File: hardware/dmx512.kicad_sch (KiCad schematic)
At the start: 18 parts, among them J16 Conn_01x06, J17 Conn_01x06, SW1 SW_DIP_x10, U4 MCP23017T-E/SS, U5 CA-IS3092W

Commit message: removed Art-Net
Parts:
- J16, J17: footprint Connector_JST:JST_PH_B6B-PH-K_1x06_P2.00mm_Vertical -> Connector_JST:JST_PH_B6B-PH-SM4-TB_1x06-1MP_P2.00mm_Vertical; LCSC C274409 -> (none)
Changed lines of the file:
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@@
 			)
 		)
-		(property "Footprint" "Connector_JST:JST_PH_B6B-PH-K_1x06_P2.00mm_Vertical"
+		(property "Footprint" "Connector_JST:JST_PH_B6B-PH-SM4-TB_1x06-1MP_P2.00mm_Vertical"
 			(at 38.1 78.74 0)
 			(effects
@@
 			)
 		)
-		(property "LCSC" "C274409"
+		(property "LCSC" ""
 			(at 38.1 78.74 0)
 			(effects
@@
 			)
 		)
-		(property "Footprint" "Connector_JST:JST_PH_B6B-PH-K_1x06_P2.00mm_Vertical"
+		(property "Footprint" "Connector_JST:JST_PH_B6B-PH-SM4-TB_1x06-1MP_P2.00mm_Vertical"
 			(at 38.1 53.34 0)
 			(effects
@@
 			)
 		)
-		(property "LCSC" "C274409"
+		(property "LCSC" ""
 			(at 38.1 53.34 0)
 			(effects

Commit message: clean up
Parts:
- added R43: 10k, Resistor_SMD:R_0603_1608Metric, symbol Device:R
- J2: renamed from J16; LCSC (none) -> C471518
- J3: renamed from J17; LCSC (none) -> C471518
- R9: renamed from R23; footprint Resistor_SMD:R_0805_2012Metric_Pad1.20x1.40mm_HandSolder -> Resistor_SMD:R_0805_2012Metric
- renumbered C23 to C10, C18 to C5, C19 to C6, C20 to C7, C21 to C8, C22 to C9, R24 to R10, R25 to R11, R26 to R12, R27 to R13, R22 to R8, U4 to U2, U5 to U3
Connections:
- net DMX_DE/~{RE}: now also R43.1
- net GND: now also R43.2
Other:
- note added: "Failsafe Bias"
- note removed: "Failsafe"

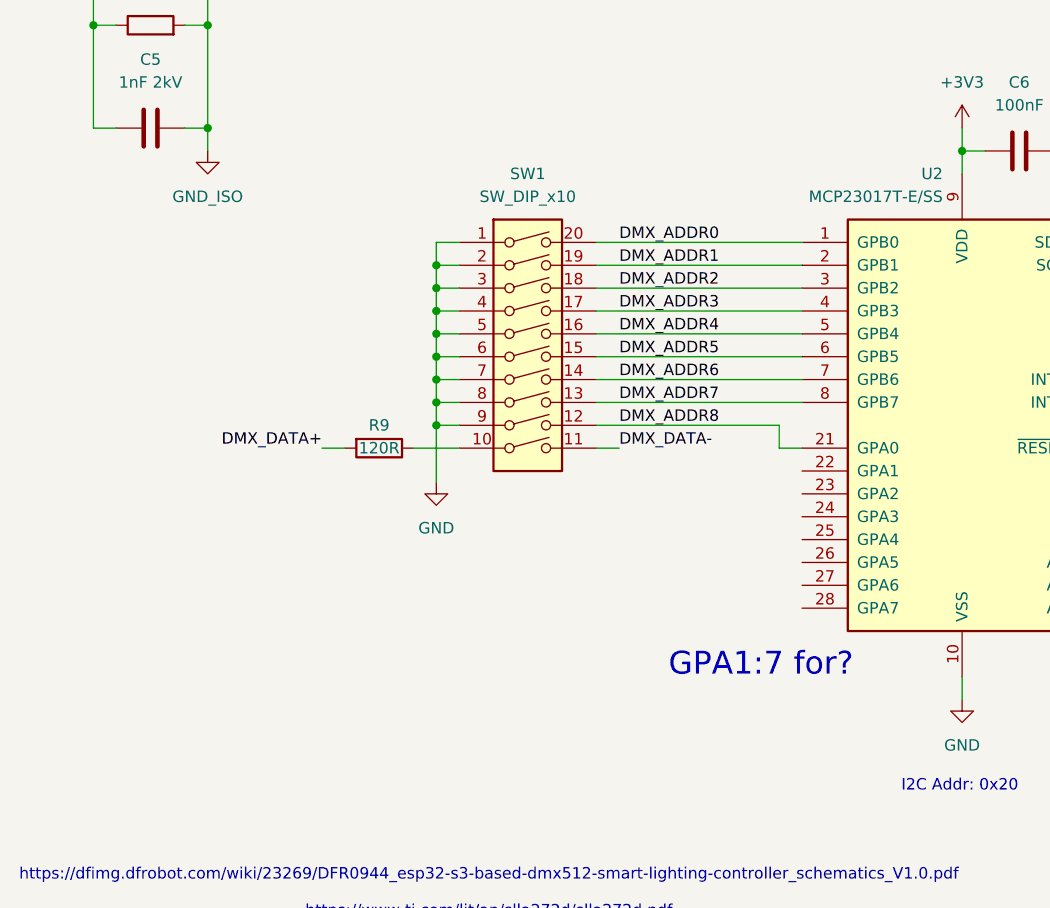
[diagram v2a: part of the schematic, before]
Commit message: updating thermistor and GPIO expander
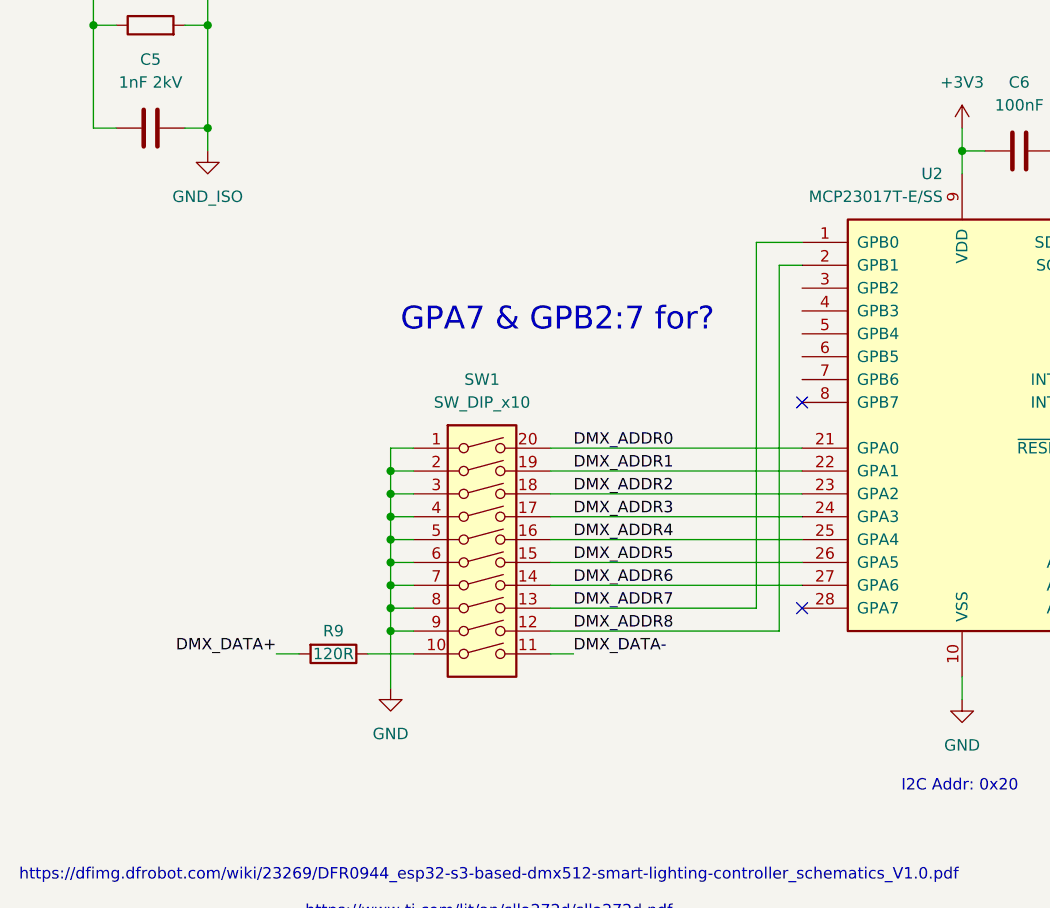
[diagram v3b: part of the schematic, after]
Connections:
- net DMX_ADDR0: now also U2.21 (GPA0); no longer U2.1 (GPB0)
- net DMX_ADDR1: now also U2.22 (GPA1); no longer U2.2 (GPB1)
- net DMX_ADDR2: now also U2.23 (GPA2); no longer U2.3 (GPB2)
- net DMX_ADDR3: now also U2.24 (GPA3); no longer U2.4 (GPB3)
- net DMX_ADDR4: now also U2.25 (GPA4); no longer U2.5 (GPB4)
- net DMX_ADDR5: now also U2.26 (GPA5); no longer U2.6 (GPB5)
- net DMX_ADDR6: now also U2.27 (GPA6); no longer U2.7 (GPB6)
- net DMX_ADDR7: now also U2.1 (GPB0); no longer U2.8 (GPB7)
- net DMX_ADDR8: now also U2.2 (GPB1); no longer U2.21 (GPA0)
- no-connect marks 1 -> 3
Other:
- note added: "GPA7 & GPB2:7 for?"
- note removed: "GPA1:7 for?"
- moved on the sheet: R9, SW1

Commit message: adding snubbers, starting placement
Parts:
- removed R9: 120R, Resistor_SMD:R_0805_2012Metric, symbol Device:R
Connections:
- net DMX_DATA-: no longer SW1.11
- net GND: now also SW1.10
- new net WIFI_~{ENABLE}: SW1.11
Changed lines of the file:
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@@
+	)
+	(junction
+		(at 78.74 165.1)
+		(diameter 0)
+		(color 0 0 0 0)
 	)
 	(junction
@@
 	(wire
 		(pts
+			(xy 194.31 38.1) (xy 194.31 40.64)
+		)
+		(stroke
+			(width 0)
+			(type default)
+		)
+	)
+	(wire
+		(pts
+			(xy 78.74 162.56) (xy 81.28 162.56)
+		)
+		(stroke
+			(width 0)
+			(type default)
+		)
+	)
+	(wire
+		(pts
+			(xy 144.78 77.47) (xy 144.78 80.01)
+		)
+		(stroke
+			(width 0)
+			(type default)
+		)
+	)
+	(wire
+		(pts
 			(xy 96.52 165.1) (xy 99.06 165.1)
 		)
@@
 	(wire
 		(pts
-			(xy 194.31 38.1) (xy 194.31 40.64)
-		)
-		(stroke
-			(width 0)
-			(type default)
-		)
-	)
-	(wire
-		(pts
-			(xy 78.74 162.56) (xy 81.28 162.56)
-		)
-		(stroke
-			(width 0)
-			(type default)
-		)
-	)
-	(wire
-		(pts
-			(xy 144.78 77.47) (xy 144.78 80.01)
+			(xy 78.74 165.1) (xy 81.28 165.1)
 		)
 		(stroke
@@
 	(wire
 		(pts
+			(xy 78.74 165.1) (xy 78.74 168.91)
+		)
+		(stroke
+			(width 0)
+			(type default)
+		)
+	)
+	(wire
+		(pts
 			(xy 58.42 95.25) (xy 58.42 73.66)
 		)
@@
 	(wire
 		(pts
-			(xy 76.2 165.1) (xy 81.28 165.1)
-		)
-		(stroke
-			(width 0)
-			(type default)
-		)
-	)
-	(wire
-		(pts
 			(xy 43.18 73.66) (xy 58.42 73.66)
 		)
@@
 	(wire
 		(pts
-			(xy 66.04 165.1) (xy 68.58 165.1)
-		)
-		(stroke
-			(width 0)
-			(type default)
-		)
-	)
-	(wire
-		(pts
 			(xy 152.4 109.22) (xy 154.94 109.22)
 		)
@@
 	(wire
 		(pts
+			(xy 99.06 167.64) (xy 101.6 167.64)
+		)
+		(stroke
+			(width 0)
+			(type default)
+		)
+	)
+	(wire
+		(pts
 			(xy 43.18 78.74) (xy 60.96 78.74)
 		)
@@
 	(wire
 		(pts
-			(xy 78.74 162.56) (xy 78.74 168.91)
+			(xy 78.74 162.56) (xy 78.74 165.1)
 		)
 		(stroke
@@
 		(pts
 			(xy 58.42 95.25) (xy 58.42 106.68)
+		)
+		(stroke
+			(width 0)
+			(type default)
+		)
+	)
+	(wire
+		(pts
+			(xy 99.06 165.1) (xy 99.06 167.64)
 		)
 		(stroke
@@
 		)
 	)
-	(label "DMX_DATA+"
-		(at 66.04 165.1 180)
-		(effects
-			(font
-				(size 1.27 1.27)
-			)
-			(justify right bottom)
-		)
-	)
 	(label "DMX_AUX+"
 		(at 60.96 83.82 0)
@@
 			)
 			(justify right bottom)
-		)
-	)
-	(label "DMX_DATA-"
-		(at 99.06 165.1 0)
-		(effects
-			(font
-				(size 1.27 1.27)
-			)
-			(justify left bottom)
 		)
 	)
@@
 		(shape output)
 		(at 226.06 72.39 0)
+		(effects
+			(font
+				(size 1.27 1.27)
+			)
+			(justify left)
+		)
+	)
+	(hierarchical_label "WIFI_~{ENABLE}"
+		(shape output)
+		(at 101.6 167.64 0)
 		(effects
 			(font
@@
 					(unit 1)
 				)
-			)
-		)
-	)
-	(symbol
-		(lib_id "Device:R")
-		(at 72.39 165.1 270)
-		(unit 1)
-		(exclude_from_sim no)
-		(in_bom yes)
-		(on_board yes)
-		(dnp no)
-		(property "Reference" "R9"
-			(at 72.39 162.56 90)
-			(effects
-				(font
-					(size 1.27 1.27)
-				)
-			)
-		)
-		(property "Value" "120R"
-			(at 72.39 165.1 90)
-			(effects
-				(font
-					(size 1.27 1.27)
-				)
-			)
-		)
-		(property "Footprint" "Resistor_SMD:R_0805_2012Metric"
-			(at 72.39 163.322 90)
-			(effects
-				(font
-					(size 1.27 1.27)
-				)
-				(hide yes)
-			)
-		)
-		(property "Datasheet" "~"
-			(at 72.39 165.1 0)
-			(effects
-				(font
-					(size 1.27 1.27)
-				)
-				(hide yes)
-			)
-		)
-		(property "Description" "Resistor"
-			(at 72.39 165.1 0)
-			(effects
-				(font
-					(size 1.27 1.27)
-				)
-				(hide yes)
-			)
-		)
-		(property "MFR" ""
-			(at 72.39 165.1 90)
-			(effects
-				(font
-					(size 1.27 1.27)
-				)
-				(hide yes)
-			)
-		)
-		(property "MPN" ""
-			(at 72.39 165.1 90)
-			(effects
-				(font
-					(size 1.27 1.27)
-				)
-				(hide yes)
-			)
-		)
-		(pin "1"
-		)
-		(pin "2"
-		)
-		(instances
-			(project "emf_beacon"
-				(path "/0654b480-d862-4382-88d5-1ac411bf5574/ef912ffd-e5d9-46a9-9fff-0bf3d4ccd370"
-					(reference "R9")
-					(unit 1)
-				)

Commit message: updating PSUs
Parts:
- C10, C7: LCSC (none) -> C15850
- C5: footprint Capacitor_SMD:C_1808_4520Metric -> Capacitor_SMD:C_1206_3216Metric; LCSC (none) -> C9196
- C6, C8, C9: LCSC (none) -> C14663
- J2, J3: Rotation_offset (none) -> 180
- R10, R11: LCSC (none) -> C23162
- R12, R13, R43: LCSC (none) -> C21190
- R8: LCSC (none) -> C17927
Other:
- note added: "Make a symbol for this"
- note added: "WiFi_~{EN} via GPIO expander?"
- note removed: "May need to actually make a symbol for this"

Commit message: some jlc cleanup
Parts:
- R12, R13, R43: LCSC C21190 -> C25804
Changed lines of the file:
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@@
 			)
 		)
-		(property "LCSC" "C21190"
+		(property "LCSC" "C25804"
 			(at 223.52 78.74 0)
 			(effects
@@
 			)
 		)
-		(property "LCSC" "C21190"
+		(property "LCSC" "C25804"
 			(at 168.91 142.24 90)
 			(effects
@@
 			)
 		)
-		(property "LCSC" "C21190"
+		(property "LCSC" "C25804"
 			(at 168.91 129.54 90)
 			(effects

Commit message: tweaking lcsc part numbers
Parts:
- C10, C7: value 10uF -> 10uF 25V
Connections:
- net +3V3: now also U3.7 (PV)
- no-connect marks 3 -> 2
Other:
- note added: "Make a symbol for CA-IS3092W CA-IS3092VW"
- note added: "OUT OF STOCK!"
- note removed: "Make a symbol for this"
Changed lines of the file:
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@@
 		(company "Wires & Bits")
 	)
-	(text "Make a symbol for this"
+	(text "Make a symbol for\nCA-IS3092W\nCA-IS3092VW"
 		(exclude_from_sim no)
 		(at 198.628 99.822 0)
@@
 		)
 	)
+	(text "OUT OF\nSTOCK!"
+		(exclude_from_sim no)
+		(at 211.074 56.896 0)
+		(effects
+			(font
+				(size 2.54 2.54)
+				(color 255 0 0 1)
+			)
+		)
+	)
 	(text "ESD\nProtection"
 		(exclude_from_sim no)
@@
 	)
 	(no_connect
-		(at 214.63 80.01)
-	)
-	(no_connect
 		(at 124.46 137.16)
 	)
@@
 	(wire
 		(pts
+			(xy 214.63 80.01) (xy 217.17 80.01)
+		)
+		(stroke
+			(width 0)
+			(type default)
+		)
+	)
+	(wire
+		(pts
 			(xy 55.88 106.68) (xy 58.42 106.68)
 		)
@@
 			)
 		)
-		(property "Value" "10uF"
+		(property "Value" "10uF 25V"
 			(at 241.3 48.2599 0)
 			(effects
@@
 	)
 	(symbol
+		(lib_id "power:+3V3")
+		(at 217.17 80.01 270)
+		(unit 1)
+		(exclude_from_sim no)
+		(in_bom yes)
+		(on_board yes)
+		(dnp no)
+		(fields_autoplaced yes)
+		(property "Reference" "#PWR073"
+			(at 213.36 80.01 0)
+			(effects
+				(font
+					(size 1.27 1.27)
+				)
+				(hide yes)
+			)
+		)
+		(property "Value" "+3V3"
+			(at 220.98 80.0099 90)
+			(effects
+				(font
+					(size 1.27 1.27)
+				)
+				(justify left)
+			)
+		)
+		(property "Footprint" ""
+			(at 217.17 80.01 0)
+			(effects
+				(font
+					(size 1.27 1.27)
+				)
+				(hide yes)
+			)
+		)
+		(property "Datasheet" ""
+			(at 217.17 80.01 0)
+			(effects
+				(font
+					(size 1.27 1.27)
+				)
+				(hide yes)
+			)
+		)
+		(property "Description" "Power symbol creates a global label with name \"+3V3\""
+			(at 217.17 80.01 0)
+			(effects
+				(font
+					(size 1.27 1.27)
+				)
+				(hide yes)
+			)
+		)
+		(pin "1"
+		)
+		(instances
+			(project "emf_beacon"
+				(path "/0654b480-d862-4382-88d5-1ac411bf5574/ef912ffd-e5d9-46a9-9fff-0bf3d4ccd370"
+					(reference "#PWR073")
+					(unit 1)
+				)
+			)
+		)
+	)
+	(symbol
 		(lib_id "Device:C")
 		(at 223.52 46.99 0)
@@
 			)
 		)
-		(property "Value" "10uF"
+		(property "Value" "10uF 25V"
 			(at 157.48 48.2599 0)
 			(effects

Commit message: general schematic and PCB clean
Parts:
- J2, J3: value Conn_01x06 -> B6B-PH-SM4-TB; symbol Connector_Generic:Conn_01x06 -> Connector_Generic_MountingPin:Conn_01x06_MountingPin
- SW1: footprint Button_Switch_THT:SW_DIP_SPSTx10_Slide_6.7x26.96mm_W7.62mm_P2.54mm_LowProfile -> Button_Switch_THT:SW_DIP_SPSTx10_Slide_9.78x27.58mm_W7.62mm_P2.54mm
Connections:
- net GND_ISO: now also J2.MP (MountPin), J3.MP (MountPin)
- net WIFI_~{ENABLE}: now also U2.3 (GPB2)
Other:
- note removed: "GPA7 & GPB2:7 for?"
- note removed: "WiFi_~{EN} via GPIO expander?"
- note removed: "https://dfimg.dfrobot.com/wiki/23269/DFR0944_esp32-s3-based-dmx512-smart-lighting-controller_schematics_V1.0.pdf https://www.ti.com/lit/an/slla272d/slla272d.pdf"
- moved on the sheet: C5, R8, SW1
